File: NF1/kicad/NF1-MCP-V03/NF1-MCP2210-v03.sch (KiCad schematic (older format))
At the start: 49 parts, among them CN1 MINIUSB, P1 TST, P2 TST, P3 TST, P4 TST, P5 TST, P6 TST, P7 TST, P8 TST, U1 BD9C301FJ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

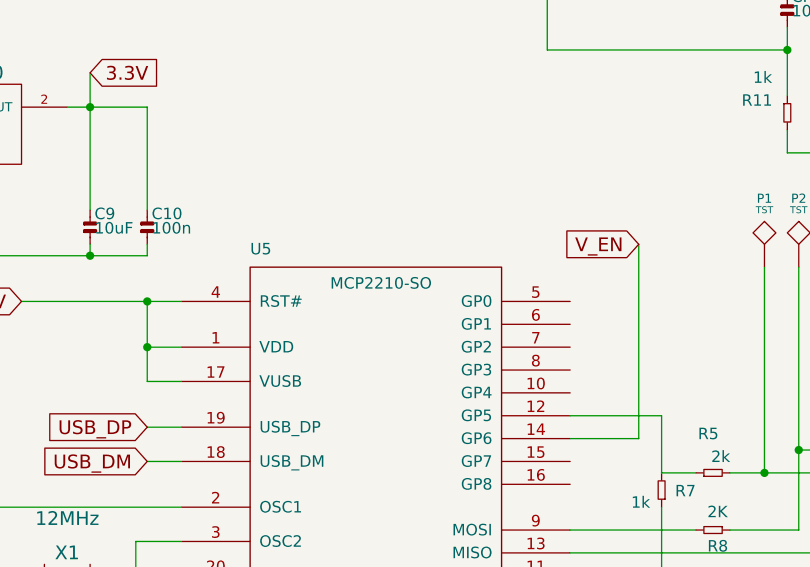
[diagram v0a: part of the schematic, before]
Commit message: update part numbers
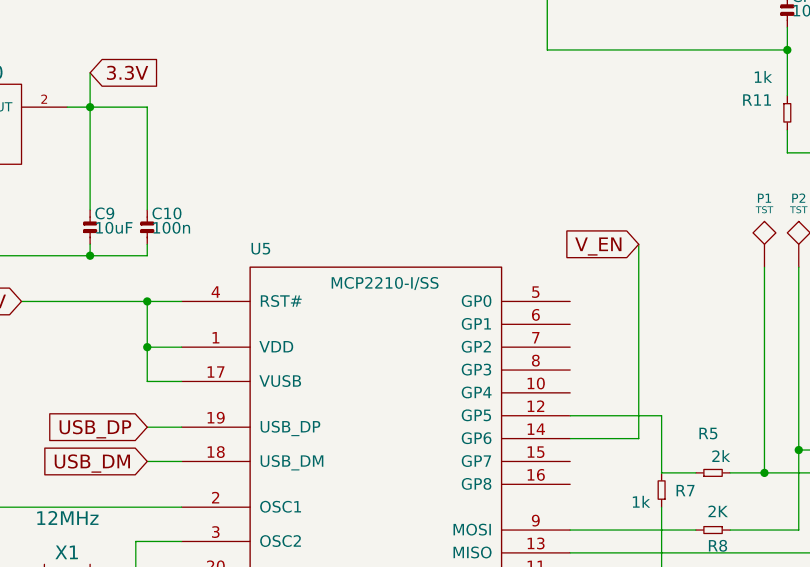
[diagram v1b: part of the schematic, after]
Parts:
- L2: DigiKey P/N (none) -> SRR1280-2R4Y
- U5: value MCP2210-SO -> MCP2210-I/SS
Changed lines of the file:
@@
 encoding utf-8
 Sheet 1 1
-Title "NanoFury NF1 - Version 1"
-Date "15 sep 2013"
-Rev "0.1"
+Title "NanoFury NF1 - Version 3"
+Date "19 sep 2013"
+Rev "0.3"
 Comp ""
 Comment1 ""
@@
 F 2 "0630" H 4900 850 60  0001 C CNN
 F 3 "" H 4950 850 60  0000 C CNN
+F 4 "SRR1280-2R4Y" H 4950 750 60  0001 C CNN "DigiKey P/N"
 	1    4950 750
 	1    0    0    -1
@@
 P 5100 3050
 F 0 "U5" H 5100 3100 50  0000 L BNN
-F 1 "MCP2210-SO" H 5450 2950 50  0000 L BNN
+F 1 "MCP2210-I/SS" H 5450 2950 50  0000 L BNN
 F 2 "SSOP-20" H 5450 2900 50  0001 L CNN
 F 3 "22288A.pdf" H 6170 1075 60  0001 C CNN
